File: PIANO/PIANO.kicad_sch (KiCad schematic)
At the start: 31 parts, among them SW1 ON/OFF, SW2 RESET, U1 LF33_TO220, U2 ESP32-WROOM-32U, U3 Opamp_Dual, U4 Opamp_Dual

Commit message: dflskdjf
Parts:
- removed U2: ESP32-WROOM-32U, RF_Module:ESP32-WROOM-32U, symbol RF_Module:ESP32-WROOM-32U
- added U2: ESP32-S2-SOLO, Espressif:ESP32-S2-SOLO, symbol Espressif:ESP32-S2-SOLO
- C1, C2: footprint (none) -> Capacitor_SMD:C_0805_2012Metric
- C3, C4, C5, C6, C7: footprint (none) -> Capacitor_SMD:C_0603_1608Metric
- D1, D2, D3: footprint (none) -> LED_THT:LED_D5.0mm-3
- LS1: footprint (none) -> Sensor_Audio:CUI_CMC-4013-SMT
- R1, R11, R2, R3, R4, R6, R8, R9: footprint (none) -> Resistor_SMD:R_0603_1608Metric
- R10, R5, R7: footprint (none) -> Resistor_SMD:R_0805_2012Metric
- RV1, RV2, RV3: footprint (none) -> Potentiometer_THT:Potentiometer_ACP_CA9-V10_Vertical
- SW1, SW2: footprint (none) -> Button_Switch_SMD:SW_DPDT_CK_JS202011JCQN
- U3, U4: footprint (none) -> Library:SOIC127P600X175-8N
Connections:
- net +3V3: now also U2.2 (3V3)
- net En: now also U2.3 (EN)
- net GND: now also U2.1 (GND)
- net IO0: now also U2.27 (GPIO0)
- net Output: now also U2.4 (GPIO4/TOUCH4/ADC1_CH3)
- net at RV2.2: now also U2.38 (GPIO2/TOUCH2/ADC1_CH1)
- net at RV1.2: now also U2.39 (GPIO1/TOUCH1/ADC1_CH0)
- net at RV3.2: now also U2.15 (GPIO3/TOUCH3/ADC1_CH2)
- no-connect marks 30 -> 36
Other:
- moved on the sheet: C5, D3, LS1, R10, R11, R8, R9, U3A, U3B, U3C

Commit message: During Class Commit
This contains all changes before design review
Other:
- note added: "Function Switch"
- note added: "Power Delivery"
- note added: "Power Switch"
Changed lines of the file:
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@@
     (stroke (width 0) (type default) (color 0 0 0 0))
+  )
+  (text "Power Delivery\n" (at 12.7 105.41 0)
+    (effects (font (size 1.27 1.27)) (justify left bottom))
+  )
+  (text "Power Switch\n" (at 48.26 151.13 0)
+    (effects (font (size 1.27 1.27)) (justify left bottom))
+  )
+  (text "Function Switch\n" (at 81.28 151.13 0)
+    (effects (font (size 1.27 1.27)) (justify left bottom))
   )
   (label "Output" (at 180.34 25.4 180)

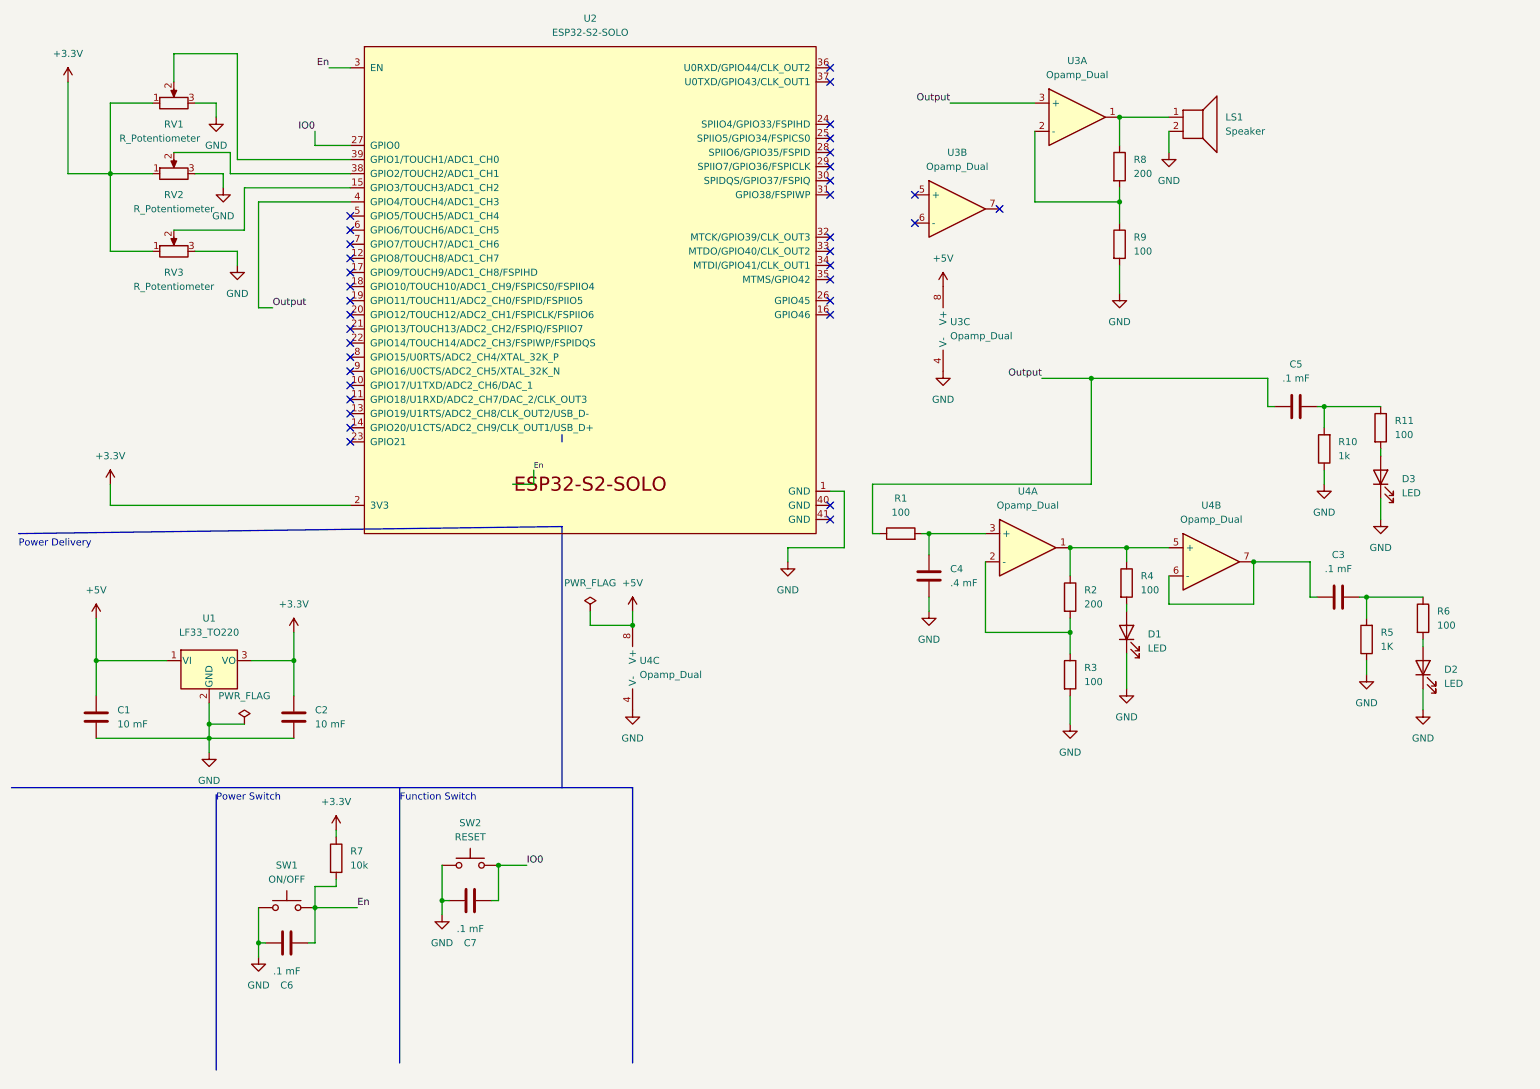
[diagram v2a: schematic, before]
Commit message: Final Handoff to Wesley
Corrected units, created exclusion, thickened traces
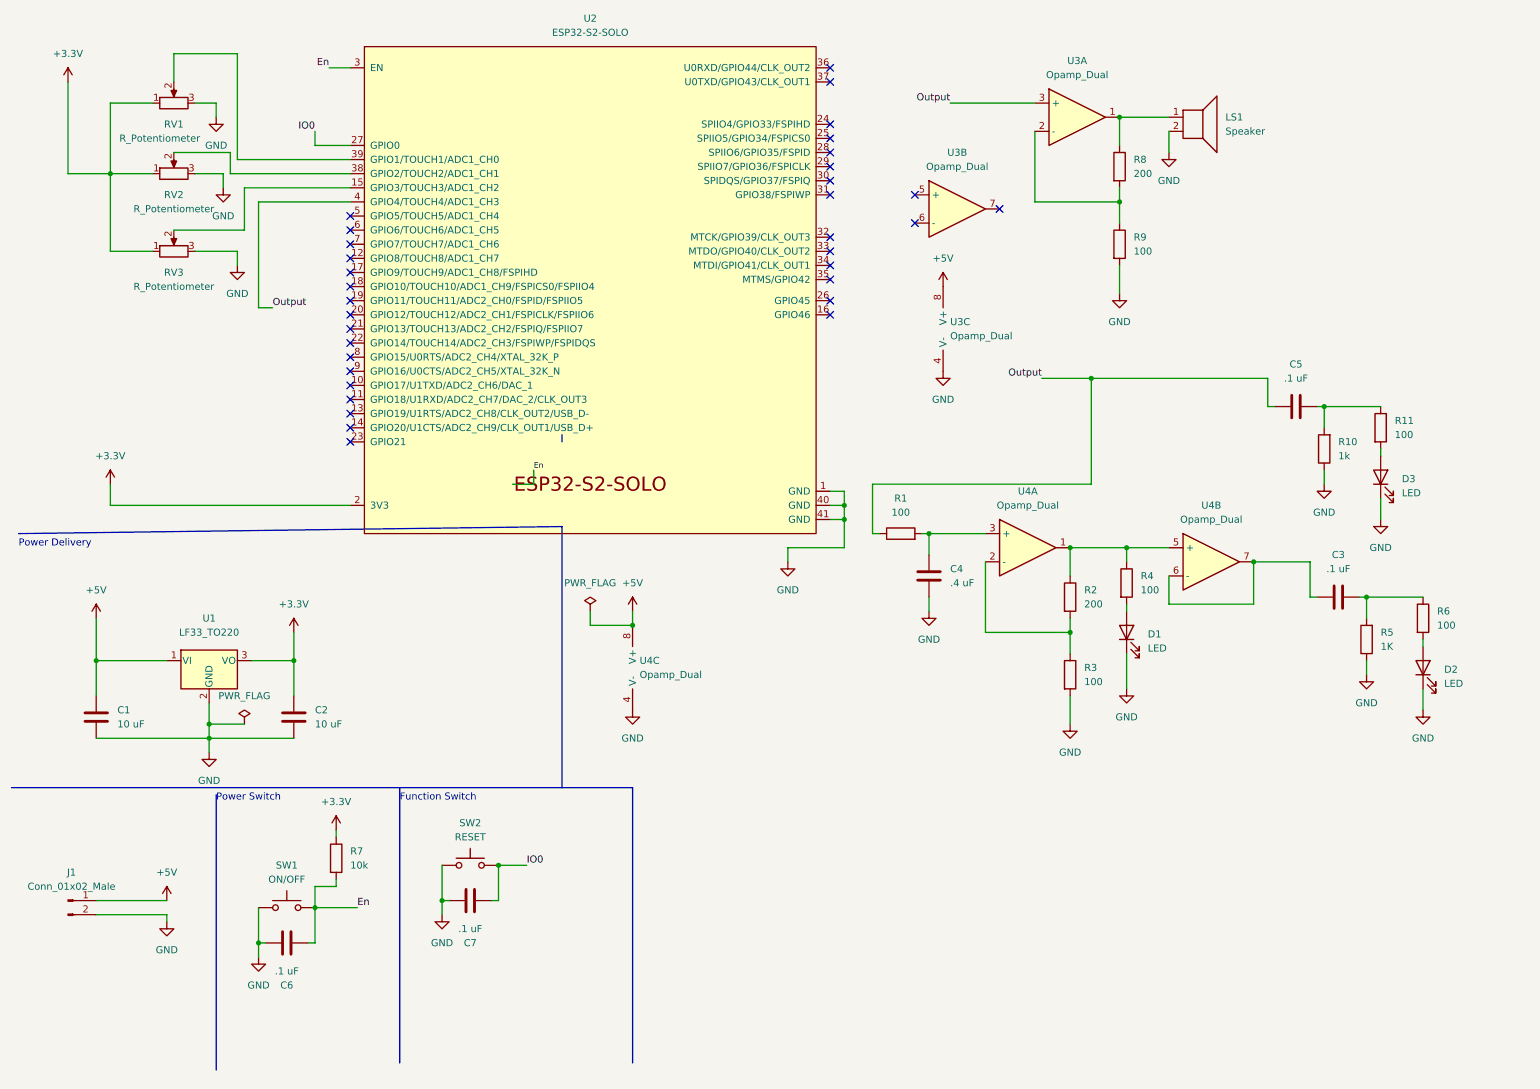
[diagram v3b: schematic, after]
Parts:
- added J1: Conn_01x02_Male, Connector_PinHeader_2.54mm:PinHeader_1x02_P2.54mm_Vertical, symbol Connector:Conn_01x02_Male
- C1, C2: value 10 mF -> 10 uF
- C3, C5, C6, C7: value .1 mF -> .1 uF
- C4: value .4 mF -> .4 uF
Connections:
- net +5V: now also J1.1 (Pin_1)
- net GND: now also U2.40 (GND), U2.41 (GND), J1.2 (Pin_2)
- no-connect marks 36 -> 34
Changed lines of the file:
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@@
   (junction (at 46.99 139.7) (diameter 0) (color 0 0 0 0)
   )
+  (junction (at 161.29 100.33) (diameter 0) (color 0 0 0 0)
+  )
   (junction (at 205.74 74.93) (diameter 0) (color 0 0 0 0)
   )
@@
   )
   (junction (at 255.27 114.3) (diameter 0) (color 0 0 0 0)
+  )
+  (junction (at 161.29 97.79) (diameter 0) (color 0 0 0 0)
   )
   (no_connect (at 189.23 44.45))
@@
   (no_connect (at 72.39 73.66))
   (no_connect (at 72.39 76.2))
-  (no_connect (at 158.75 97.79))
-  (no_connect (at 158.75 100.33))
   (no_connect (at 158.75 41.91))
   (no_connect (at 158.75 49.53))
@@
     (stroke (width 0) (type default) (color 0 0 0 0))
   )
+  (wire (pts (xy 161.29 97.79) (xy 161.29 95.25))
+    (stroke (width 0) (type default) (color 0 0 0 0))
+  )
   (wire (pts (xy 201.93 105.41) (xy 212.09 105.41))
     (stroke (width 0) (type default) (color 0 0 0 0))
@@
     (stroke (width 0) (type default) (color 0 0 0 0))
   )
+  (wire (pts (xy 26.67 171.45) (xy 39.37 171.45))
+    (stroke (width 0) (type default) (color 0 0 0 0))
+  )
   (wire (pts (xy 115.57 116.84) (xy 115.57 119.38))
     (stroke (width 0) (type default) (color 0 0 0 0))
@@
     (stroke (width 0) (type default) (color 0 0 0 0))
   )
+  (wire (pts (xy 39.37 171.45) (xy 39.37 172.72))
+    (stroke (width 0) (type default) (color 0 0 0 0))
+  )
   (wire (pts (xy 52.07 35.56) (xy 72.39 35.56))
     (stroke (width 0) (type default) (color 0 0 0 0))
@@
     (stroke (width 0) (type default) (color 0 0 0 0))
   )
+  (wire (pts (xy 26.67 168.91) (xy 39.37 168.91))
+    (stroke (width 0) (type default) (color 0 0 0 0))
+  )
   (wire (pts (xy 219.71 30.48) (xy 219.71 34.29))
     (stroke (width 0) (type default) (color 0 0 0 0))
@@
     (stroke (width 0) (type default) (color 0 0 0 0))
   )
+  (wire (pts (xy 158.75 100.33) (xy 161.29 100.33))
+    (stroke (width 0) (type default) (color 0 0 0 0))
+  )
   (wire (pts (xy 29.21 52.07) (xy 36.83 52.07))
     (stroke (width 0) (type default) (color 0 0 0 0))
@@
     (stroke (width 0) (type default) (color 0 0 0 0))
   )
+  (wire (pts (xy 158.75 97.79) (xy 161.29 97.79))
+    (stroke (width 0) (type default) (color 0 0 0 0))
+  )
   (wire (pts (xy 40.64 21.59) (xy 40.64 16.51))
     (stroke (width 0) (type default) (color 0 0 0 0))
@@
     (stroke (width 0) (type default) (color 0 0 0 0))
   )
-  (wire (pts (xy 161.29 105.41) (xy 161.29 95.25))
+  (wire (pts (xy 161.29 105.41) (xy 161.29 100.33))
     (stroke (width 0) (type default) (color 0 0 0 0))
   )
   (wire (pts (xy 64.77 176.53) (xy 66.04 176.53))
+    (stroke (width 0) (type default) (color 0 0 0 0))
+  )
+  (wire (pts (xy 161.29 100.33) (xy 161.29 97.79))
     (stroke (width 0) (type default) (color 0 0 0 0))
   )
@@
       (effects (font (size 1.27 1.27)) (justify left))
     )
-    (property "Value" ".4 mF" (id 1) (at 180.34 111.7599 0)
+    (property "Value" ".4 uF" (id 1) (at 180.34 111.7599 0)
       (effects (font (size 1.27 1.27)) (justify left))
     )
@@
     (in_bom yes) (on_board yes)
     (property "Reference" "C6" (id 0) (at 60.96 184.15 90))
-    (property "Value" ".1 mF" (id 1) (at 60.96 181.61 90))
+    (property "Value" ".1 uF" (id 1) (at 60.96 181.61 90))
     (property "Footprint" "Capacitor_SMD:C_0603_1608Metric" (id 2) (at 64.77 175.5648 0)
       (effects (font (size 1.27 1.27)) hide)
@@
       (effects (font (size 1.27 1.27)) (justify left))
     )
-    (property "Value" "10 mF" (id 1) (at 66.04 137.1599 0)
+    (property "Value" "10 uF" (id 1) (at 66.04 137.1599 0)
       (effects (font (size 1.27 1.27)) (justify left))
     )
@@
     (in_bom yes) (on_board yes) (fields_autoplaced)
     (property "Reference" "C5" (id 0) (at 242.57 72.39 90))
-    (property "Value" ".1 mF" (id 1) (at 242.57 74.93 90))
+    (property "Value" ".1 uF" (id 1) (at 242.57 74.93 90))
     (property "Footprint" "Capacitor_SMD:C_0603_1608Metric" (id 2) (at 246.38 79.0448 0)
       (effects (font (size 1.27 1.27)) hide)
@@
     (in_bom yes) (on_board yes) (fields_autoplaced)
     (property "Reference" "C3" (id 0) (at 250.19 106.68 90))
-    (property "Value" ".1 mF" (id 1) (at 250.19 109.22 90))
+    (property "Value" ".1 uF" (id 1) (at 250.19 109.22 90))
     (property "Footprint" "Capacitor_SMD:C_0603_1608Metric" (id 2) (at 254 113.3348 0)
       (effects (font (size 1.27 1.27)) hide)
@@
     (pin "1")
     (pin "2")
+  )
+  (symbol (lib_id "power:+5V") (at 39.37 168.91 0) (unit 1)
+    (in_bom yes) (on_board yes) (fields_autoplaced)
+    (property "Reference" "#PWR0126" (id 0) (at 39.37 172.72 0)
+      (effects (font (size 1.27 1.27)) hide)
+    )
+    (property "Value" "+5V" (id 1) (at 39.37 163.83 0))
+    (property "Footprint" "" (id 2) (at 39.37 168.91 0)
+      (effects (font (size 1.27 1.27)) hide)
+    )
+    (property "Datasheet" "" (id 3) (at 39.37 168.91 0)
+      (effects (font (size 1.27 1.27)) hide)
+    )
+    (pin "1")
   )
   (symbol (lib_id "Switch:SW_Push") (at 60.96 170.18 0) (unit 1)
@@
     (pin "7")
   )
+  (symbol (lib_id "power:GND") (at 39.37 172.72 0) (unit 1)
+    (in_bom yes) (on_board yes) (fields_autoplaced)
+    (property "Reference" "#PWR0127" (id 0) (at 39.37 179.07 0)
+      (effects (font (size 1.27 1.27)) hide)
+    )
+    (property "Value" "GND" (id 1) (at 39.37 177.8 0))
+    (property "Footprint" "" (id 2) (at 39.37 172.72 0)
+      (effects (font (size 1.27 1.27)) hide)
+    )
+    (property "Datasheet" "" (id 3) (at 39.37 172.72 0)
+      (effects (font (size 1.27 1.27)) hide)
+    )
+    (pin "1")
+  )
   (symbol (lib_id "Device:C") (at 26.67 135.89 0) (unit 1)
     (in_bom yes) (on_board yes) (fields_autoplaced)
@@
       (effects (font (size 1.27 1.27)) (justify left))
     )
-    (property "Value" "10 mF" (id 1) (at 30.48 137.1599 0)
+    (property "Value" "10 uF" (id 1) (at 30.48 137.1599 0)
       (effects (font (size 1.27 1.27)) (justify left))
     )
@@
     (in_bom yes) (on_board yes)
     (property "Reference" "C7" (id 0) (at 93.98 176.53 90))
-    (property "Value" ".1 mF" (id 1) (at 93.98 173.99 90))
+    (property "Value" ".1 uF" (id 1) (at 93.98 173.99 90))
     (property "Footprint" "Capacitor_SMD:C_0603_1608Metric" (id 2) (at 97.79 167.9448 0)
       (effects (font (size 1.27 1.27)) hide)
@@
     (pin "3")
   )
+  (symbol (lib_id "Connector:Conn_01x02_Male") (at 21.59 168.91 0) (unit 1)
+    (in_bom yes) (on_board yes) (fields_autoplaced)
+    (property "Reference" "J1" (id 0) (at 22.225 163.83 0))
+    (property "Value" "Conn_01x02_Male" (id 1) (at 22.225 166.37 0))
+    (property "Footprint" "Connector_PinHeader_2.54mm:PinHeader_1x02_P2.54mm_Vertical" (id 2) (at 21.59 168.91 0)
+      (effects (font (size 1.27 1.27)) hide)
+    )
+    (property "Datasheet" "~" (id 3) (at 21.59 168.91 0)
+      (effects (font (size 1.27 1.27)) hide)
+    )
+    (pin "1")
+    (pin "2")
+  )
   (symbol (lib_id "power:+3.3V") (at 29.21 93.98 0) (unit 1)
     (in_bom yes) (on_board yes) (fields_autoplaced)
@@
       (reference "#PWR0125") (unit 1) (value "GND") (footprint "")
     )
+    (path "/6d0fcfab-1489-4b20-9a6e-8f03fde820ca"
+      (reference "#PWR0126") (unit 1) (value "+5V") (footprint "")
+    )
+    (path "/7b0390e3-cb04-40a0-8a44-04ff72f542fb"
+      (reference "#PWR0127") (unit 1) (value "GND") (footprint "")
+    )
     (path "/7f05d072-22d9-4098-ad43-15fc4a4844a4"
-      (reference "C1") (unit 1) (value "10 mF") (footprint "Capacitor_SMD:C_0805_2012Metric")
+      (reference "C1") (unit 1) (value "10 uF") (footprint "Capacitor_SMD:C_0805_2012Metric")
     )
     (path "/4d04e639-00e2-4298-ab27-52b8d7f66e24"
-      (reference "C2") (unit 1) (value "10 mF") (footprint "Capacitor_SMD:C_0805_2012Metric")
+      (reference "C2") (unit 1) (value "10 uF") (footprint "Capacitor_SMD:C_0805_2012Metric")
     )
     (path "/6acd08c9-2a3f-4566-8d90-a3c51a175bb8"
-      (reference "C3") (unit 1) (value ".1 mF") (footprint "Capacitor_SMD:C_0603_1608Metric")
+      (reference "C3") (unit 1) (value ".1 uF") (footprint "Capacitor_SMD:C_0603_1608Metric")
     )
     (path "/0f2d9f25-9bbc-4233-9c4a-edef7077fe86"
-      (reference "C4") (unit 1) (value ".4 mF") (footprint "Capacitor_SMD:C_0603_1608Metric")
+      (reference "C4") (unit 1) (value ".4 uF") (footprint "Capacitor_SMD:C_0603_1608Metric")
     )
     (path "/653a4a14-5e47-4217-b538-2d6db2e974fe"
-      (reference "C5") (unit 1) (value ".1 mF") (footprint "Capacitor_SMD:C_0603_1608Metric")
+      (reference "C5") (unit 1) (value ".1 uF") (footprint "Capacitor_SMD:C_0603_1608Metric")
     )
     (path "/29af9c27-510c-4dd5-9482-44c1ecf8193f"
-      (reference "C6") (unit 1) (value ".1 mF") (footprint "Capacitor_SMD:C_0603_1608Metric")
+      (reference "C6") (unit 1) (value ".1 uF") (footprint "Capacitor_SMD:C_0603_1608Metric")
     )
     (path "/a554e561-29d7-4ec7-aac3-7b0336190a90"
-      (reference "C7") (unit 1) (value ".1 mF") (footprint "Capacitor_SMD:C_0603_1608Metric")
+      (reference "C7") (unit 1) (value ".1 uF") (footprint "Capacitor_SMD:C_0603_1608Metric")
     )
     (path "/1cc8da2d-620e-4e25-8400-5114364ff5fc"
@@
       (reference "D3") (unit 1) (value "LED") (footprint "LED_THT:LED_D5.0mm-3")
     )
+    (path "/a8eec9a6-5455-454a-8104-384cf0571e04"
+      (reference "J1") (unit 1) (value "Conn_01x02_Male") (footprint "Connector_PinHeader_2.54mm:PinHeader_1x02_P2.54mm_Vertical")
+    )
     (path "/fa5d73d3-725e-46cd-832f-91c3aae99215"

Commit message: New Power Delivery
Created new switching regulator and respective passives.
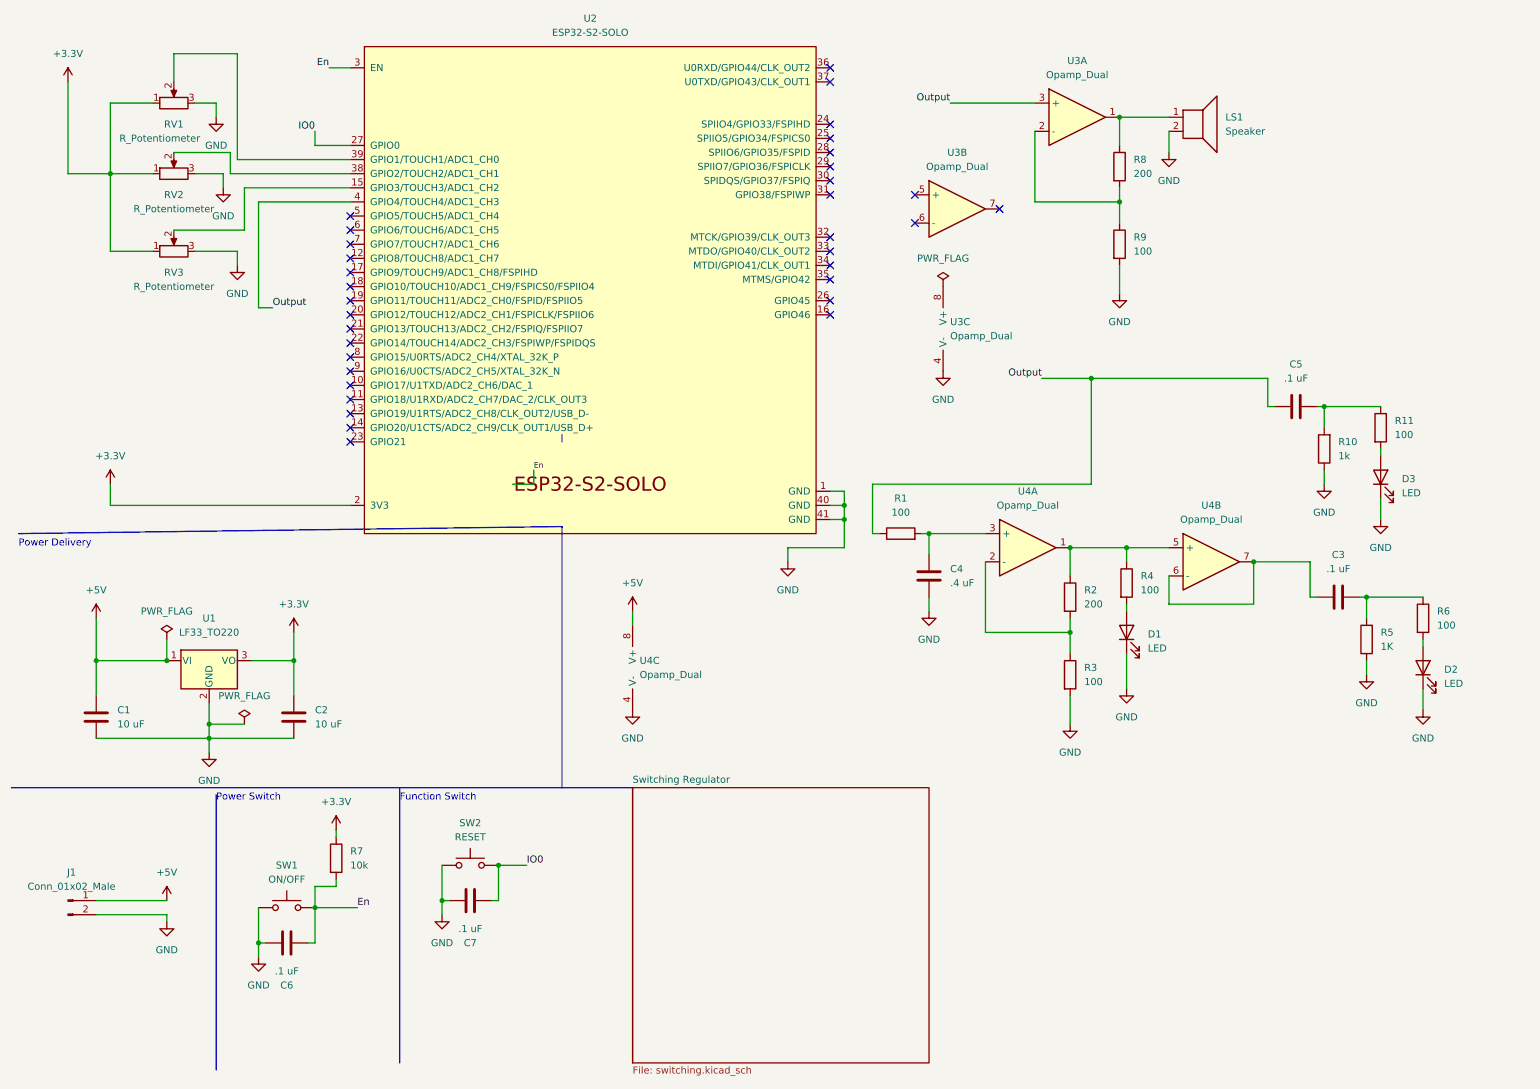
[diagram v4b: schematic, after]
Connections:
- net +5V: no longer U3.8 (V+)
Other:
- added sheet Switching Regulator (switching.kicad_sch)
